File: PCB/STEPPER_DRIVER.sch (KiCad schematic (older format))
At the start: 12 parts, among them J3 STEPPER, J4 STEPPER, U3 DRV8825_BREAKOUT

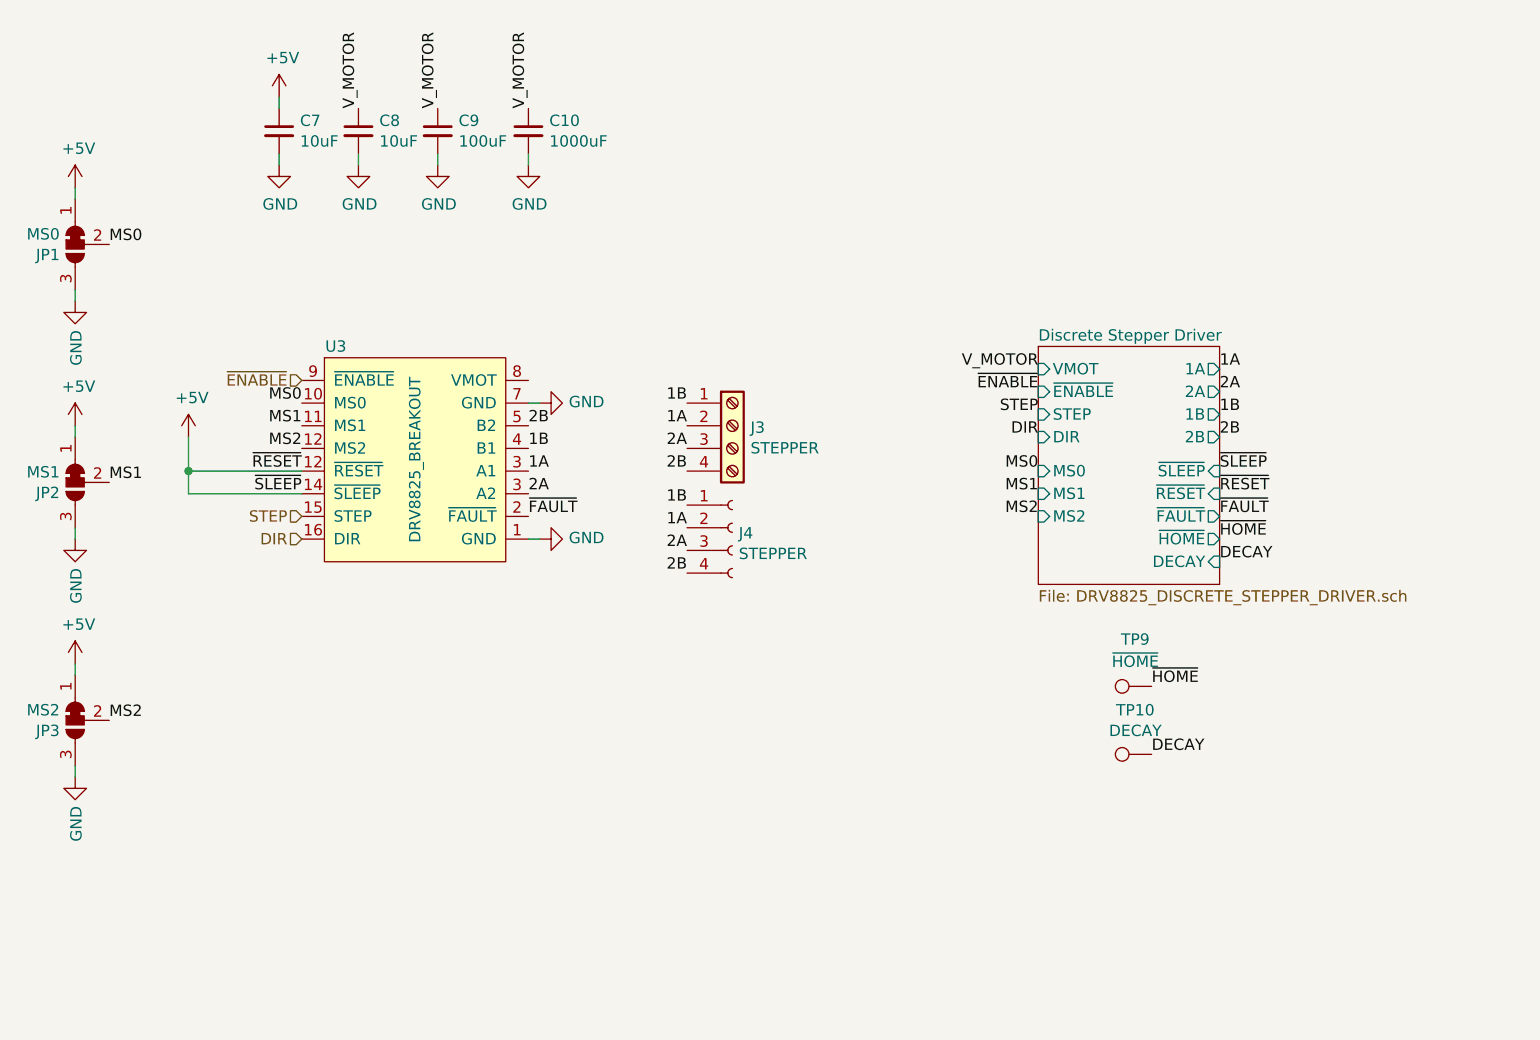
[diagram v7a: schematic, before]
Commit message: Added majority footprints
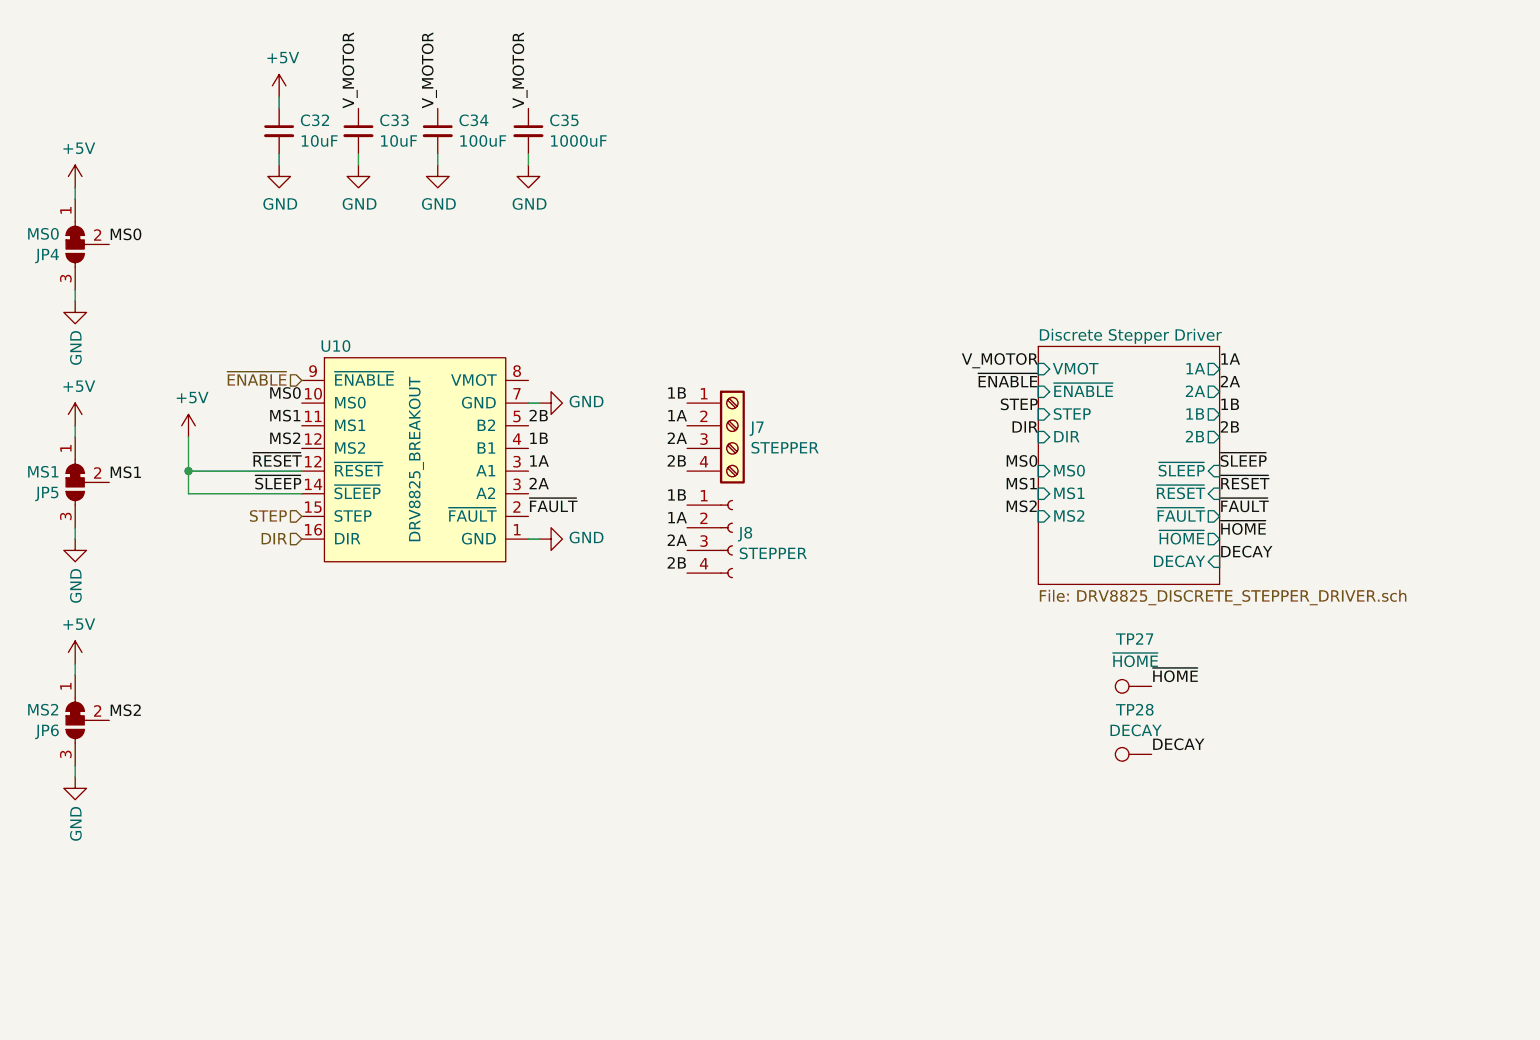
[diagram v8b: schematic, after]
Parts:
- C10: footprint (none) -> Capacitor_SMD:CP_Elec_8x10
- C7, C8: footprint (none) -> Capacitor_SMD:C_0603_1608Metric
- J4: footprint (none) -> Connector_Molex:Molex_KK-254_AE-6410-04A_1x04_P2.54mm_Vertical
- TP10, TP9: footprint (none) -> custom:TestPoint_Pad_D1.5mm
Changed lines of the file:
@@
 $Descr A4 11693 8268
 encoding utf-8
-Sheet 3 22
+Sheet 14 22
 Title ""
 Date ""
@@
 AR Path="/5E8A6686/5E8A7820" Ref="J4"  Part="1"
 AR Path="/5E8813FF/5E8A7820" Ref="J8"  Part="1"
-F 0 "J4" H 7278 4226 50  0000 L CNN
+F 0 "J8" H 7278 4226 50  0000 L CNN
 F 1 "STEPPER" H 7278 4135 50  0000 L CNN
-F 2 "" H 7250 4250 50  0001 C CNN
+F 2 "Connector_Molex:Molex_KK-254_AE-6410-04A_1x04_P2.54mm_Vertical" H 7250 4250 50  0001 C CNN
 F 3 "" H 7250 4250 50  0001 C CNN
 	1    7250 4250
@@
 AR Path="/5E8A6686/5E8A82D9" Ref="J3"  Part="1"
 AR Path="/5E8813FF/5E8A82D9" Ref="J7"  Part="1"
-F 0 "J3" H 7330 3792 50  0000 L CNN
+F 0 "J7" H 7330 3792 50  0000 L CNN
 F 1 "STEPPER" H 7330 3701 50  0000 L CNN
 F 2 "" H 7250 3800 50  0001 C CNN
@@
 AR Path="/5E8A6686/5E842853" Ref="#PWR038"  Part="1"
 AR Path="/5E8813FF/5E842853" Ref="#PWR0103"  Part="1"
-F 0 "#PWR038" H 6400 4050 50  0001 C CNN
+F 0 "#PWR0103" H 6400 4050 50  0001 C CNN
 F 1 "GND" V 6405 4172 50  0000 R CNN
 F 2 "" H 6400 4300 50  0001 C CNN
@@
 AR Path="/5E8A6686/5E842AD6" Ref="#PWR037"  Part="1"
 AR Path="/5E8813FF/5E842AD6" Ref="#PWR0102"  Part="1"
-F 0 "#PWR037" H 6400 3450 50  0001 C CNN
+F 0 "#PWR0102" H 6400 3450 50  0001 C CNN
 F 1 "GND" V 6405 3572 50  0000 R CNN
 F 2 "" H 6400 3700 50  0001 C CNN
@@
 AR Path="/5E8A6686/5E8548E0" Ref="C9"  Part="1"
 AR Path="/5E8813FF/5E8548E0" Ref="C34"  Part="1"
-F 0 "C9" H 6042 2546 50  0000 L CNN
+F 0 "C34" H 6042 2546 50  0000 L CNN
 F 1 "100uF" H 6042 2455 50  0000 L CNN
 F 2 "" H 5950 2500 50  0001 C CNN
@@
 AR Path="/5E8A6686/5E8548E7" Ref="#PWR035"  Part="1"
 AR Path="/5E8813FF/5E8548E7" Ref="#PWR0100"  Part="1"
-F 0 "#PWR035" H 5950 2400 50  0001 C CNN
+F 0 "#PWR0100" H 5950 2400 50  0001 C CNN
 F 1 "GND" H 5955 2477 50  0000 C CNN
 F 2 "" H 5950 2650 50  0001 C CNN
@@
 AR Path="/5E8A6686/5E8572F7" Ref="C8"  Part="1"
 AR Path="/5E8813FF/5E8572F7" Ref="C33"  Part="1"
-F 0 "C8" H 5692 2546 50  0000 L CNN
+F 0 "C33" H 5692 2546 50  0000 L CNN
 F 1 "10uF" H 5692 2455 50  0000 L CNN
-F 2 "" H 5600 2500 50  0001 C CNN
+F 2 "Capacitor_SMD:C_0603_1608Metric" H 5600 2500 50  0001 C CNN
 F 3 "" H 5600 2500 50  0001 C CNN
 F 4 "50V" H 5600 2500 50  0001 C CNN "Voltage Rating"
@@
 AR Path="/5E8A6686/5E8572FE" Ref="#PWR034"  Part="1"
 AR Path="/5E8813FF/5E8572FE" Ref="#PWR099"  Part="1"
-F 0 "#PWR034" H 5600 2400 50  0001 C CNN
+F 0 "#PWR099" H 5600 2400 50  0001 C CNN
 F 1 "GND" H 5605 2477 50  0000 C CNN
 F 2 "" H 5600 2650 50  0001 C CNN
@@
 AR Path="/5E8A6686/5E860421" Ref="C7"  Part="1"
 AR Path="/5E8813FF/5E860421" Ref="C32"  Part="1"
-F 0 "C7" H 5342 2546 50  0000 L CNN
+F 0 "C32" H 5342 2546 50  0000 L CNN
 F 1 "10uF" H 5342 2455 50  0000 L CNN
-F 2 "" H 5250 2500 50  0001 C CNN
+F 2 "Capacitor_SMD:C_0603_1608Metric" H 5250 2500 50  0001 C CNN
 F 3 "" H 5250 2500 50  0001 C CNN
 F 4 "6.3V" H 5250 2500 50  0001 C CNN "Voltage Rating"
@@
 AR Path="/5E8A6686/5E860428" Ref="#PWR033"  Part="1"
 AR Path="/5E8813FF/5E860428" Ref="#PWR098"  Part="1"
-F 0 "#PWR033" H 5250 2400 50  0001 C CNN
+F 0 "#PWR098" H 5250 2400 50  0001 C CNN
 F 1 "GND" H 5255 2477 50  0000 C CNN
 F 2 "" H 5250 2650 50  0001 C CNN
@@
 AR Path="/5E8A6686/5E90606A" Ref="#PWR032"  Part="1"
 AR Path="/5E8813FF/5E90606A" Ref="#PWR097"  Part="1"
-F 0 "#PWR032" H 5250 2200 50  0001 C CNN
+F 0 "#PWR097" H 5250 2200 50  0001 C CNN
 F 1 "+5V" H 5265 2523 50  0000 C CNN
 F 2 "" H 5250 2350 50  0001 C CNN
@@
 AR Path="/5E8A6686/5E85775C" Ref="#PWR036"  Part="1"
 AR Path="/5E8813FF/5E85775C" Ref="#PWR0101"  Part="1"
-F 0 "#PWR036" H 6350 2400 50  0001 C CNN
+F 0 "#PWR0101" H 6350 2400 50  0001 C CNN
 F 1 "GND" H 6355 2477 50  0000 C CNN
 F 2 "" H 6350 2650 50  0001 C CNN
@@
 AR Path="/5E8A6686/5E857755" Ref="C10"  Part="1"
 AR Path="/5E8813FF/5E857755" Ref="C35"  Part="1"
-F 0 "C10" H 6442 2546 50  0000 L CNN
+F 0 "C35" H 6442 2546 50  0000 L CNN
 F 1 "1000uF" H 6442 2455 50  0000 L CNN
-F 2 "" H 6350 2500 50  0001 C CNN
+F 2 "Capacitor_SMD:CP_Elec_8x10" H 6350 2500 50  0001 C CNN
 F 3 "" H 6350 2500 50  0001 C CNN
 F 4 "50V" H 6350 2500 50  0001 C CNN "Voltage Rating"
@@
 AR Path="/5E8A6686/5E913339" Ref="JP1"  Part="1"
 AR Path="/5E8813FF/5E913339" Ref="JP4"  Part="1"
-F 0 "JP1" V 4396 3068 50  0000 L CNN
+F 0 "JP4" V 4396 3068 50  0000 L CNN
 F 1 "MS0" V 4305 3068 50  0000 L CNN
 F 2 "Jumpers:SMT-JUMPER_3_1-NC_PASTE_SILK" H 4350 3000 50  0001 C CNN
@@
 AR Path="/5E8A6686/5E9143CE" Ref="#PWR025"  Part="1"
 AR Path="/5E8813FF/5E9143CE" Ref="#PWR090"  Part="1"
-F 0 "#PWR025" H 4350 2600 50  0001 C CNN
+F 0 "#PWR090" H 4350 2600 50  0001 C CNN
 F 1 "+5V" H 4365 2923 50  0000 C CNN
 F 2 "" H 4350 2750 50  0001 C CNN
@@
 AR Path="/5E8A6686/5E914CAC" Ref="#PWR026"  Part="1"
 AR Path="/5E8813FF/5E914CAC" Ref="#PWR091"  Part="1"
-F 0 "#PWR026" H 4350 3000 50  0001 C CNN
+F 0 "#PWR091" H 4350 3000 50  0001 C CNN
 F 1 "GND" V 4355 3122 50  0000 R CNN
 F 2 "" H 4350 3250 50  0001 C CNN
@@
 AR Path="/5E8A6686/5E916887" Ref="JP2"  Part="1"
 AR Path="/5E8813FF/5E916887" Ref="JP5"  Part="1"
-F 0 "JP2" V 4396 4118 50  0000 L CNN
+F 0 "JP5" V 4396 4118 50  0000 L CNN
 F 1 "MS1" V 4305 4118 50  0000 L CNN
 F 2 "Jumpers:SMT-JUMPER_3_1-NC_PASTE_SILK" H 4350 4050 50  0001 C CNN
@@
 AR Path="/5E8A6686/5E91688D" Ref="#PWR027"  Part="1"
 AR Path="/5E8813FF/5E91688D" Ref="#PWR092"  Part="1"
-F 0 "#PWR027" H 4350 3650 50  0001 C CNN
+F 0 "#PWR092" H 4350 3650 50  0001 C CNN
 F 1 "+5V" H 4365 3973 50  0000 C CNN
 F 2 "" H 4350 3800 50  0001 C CNN
@@
 AR Path="/5E8A6686/5E916894" Ref="#PWR028"  Part="1"
 AR Path="/5E8813FF/5E916894" Ref="#PWR093"  Part="1"
-F 0 "#PWR028" H 4350 4050 50  0001 C CNN
+F 0 "#PWR093" H 4350 4050 50  0001 C CNN
 F 1 "GND" V 4355 4172 50  0000 R CNN
 F 2 "" H 4350 4300 50  0001 C CNN
@@
 AR Path="/5E8A6686/5E917232" Ref="JP3"  Part="1"
 AR Path="/5E8813FF/5E917232" Ref="JP6"  Part="1"
-F 0 "JP3" V 4396 5168 50  0000 L CNN
+F 0 "JP6" V 4396 5168 50  0000 L CNN
 F 1 "MS2" V 4305 5168 50  0000 L CNN
 F 2 "Jumpers:SMT-JUMPER_3_1-NC_PASTE_SILK" H 4350 5100 50  0001 C CNN
@@
 AR Path="/5E8A6686/5E917238" Ref="#PWR029"  Part="1"
 AR Path="/5E8813FF/5E917238" Ref="#PWR094"  Part="1"
-F 0 "#PWR029" H 4350 4700 50  0001 C CNN
+F 0 "#PWR094" H 4350 4700 50  0001 C CNN
 F 1 "+5V" H 4365 5023 50  0000 C CNN
 F 2 "" H 4350 4850 50  0001 C CNN
@@
 AR Path="/5E8A6686/5E91723F" Ref="#PWR030"  Part="1"
 AR Path="/5E8813FF/5E91723F" Ref="#PWR095"  Part="1"
-F 0 "#PWR030" H 4350 5100 50  0001 C CNN
+F 0 "#PWR095" H 4350 5100 50  0001 C CNN
 F 1 "GND" V 4355 5222 50  0000 R CNN
 F 2 "" H 4350 5350 50  0001 C CNN
@@
 AR Path="/5E8A6686/5E952808" Ref="#PWR031"  Part="1"
 AR Path="/5E8813FF/5E952808" Ref="#PWR096"  Part="1"
-F 0 "#PWR031" H 4850 3700 50  0001 C CNN
+F 0 "#PWR096" H 4850 3700 50  0001 C CNN
 F 1 "+5V" H 4865 4023 50  0000 C CNN
 F 2 "" H 4850 3850 50  0001 C CNN
@@
 AR Path="/5E8A6686/5E972E18" Ref="U3"  Part="1"
 AR Path="/5E8813FF/5E972E18" Ref="U10"  Part="1"
-F 0 "U3" H 5500 4450 50  0000 C CNN
+F 0 "U10" H 5500 4450 50  0000 C CNN
 F 1 "DRV8825_BREAKOUT" V 5850 3950 50  0000 C CNN
 F 2 "Module:Pololu_Breakout-16_15.2x20.3mm" H 6000 3900 50  0001 C CNN
@@
 AR Path="/5E8A6686/5E998E64" Ref="TP9"  Part="1"
 AR Path="/5E8813FF/5E998E64" Ref="TP27"  Part="1"
-F 0 "TP9" V 9307 5022 50  0000 C CNN
+F 0 "TP27" V 9307 5022 50  0000 C CNN
 F 1 "~HOME" V 9209 5022 50  0000 C CNN
-F 2 "" H 9300 4950 50  0001 C CNN
+F 2 "custom:TestPoint_Pad_D1.5mm" H 9300 4950 50  0001 C CNN
 F 3 "~" H 9300 4950 50  0001 C CNN
 	1    9100 4950
@@
 AR Path="/5E8A6686/5E99966E" Ref="TP10"  Part="1"
 AR Path="/5E8813FF/5E99966E" Ref="TP28"  Part="1"
-F 0 "TP10" V 9295 5322 50  0000 C CNN
+F 0 "TP28" V 9295 5322 50  0000 C CNN
 F 1 "DECAY" V 9204 5322 50  0000 C CNN
-F 2 "" H 9300 5250 50  0001 C CNN
+F 2 "custom:TestPoint_Pad_D1.5mm" H 9300 5250 50  0001 C CNN
 F 3 "~" H 9300 5250 50  0001 C CNN
 	1    9100 5250
